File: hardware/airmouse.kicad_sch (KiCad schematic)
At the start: 25 parts, among them J1 USB_C_Receptacle_USB2.0_16P, J2 Conn_01x07_Pin, U1 XC6206PxxxMR, U2 MPU-9250, U3 STM32F103CBTx, Y1 8MHz

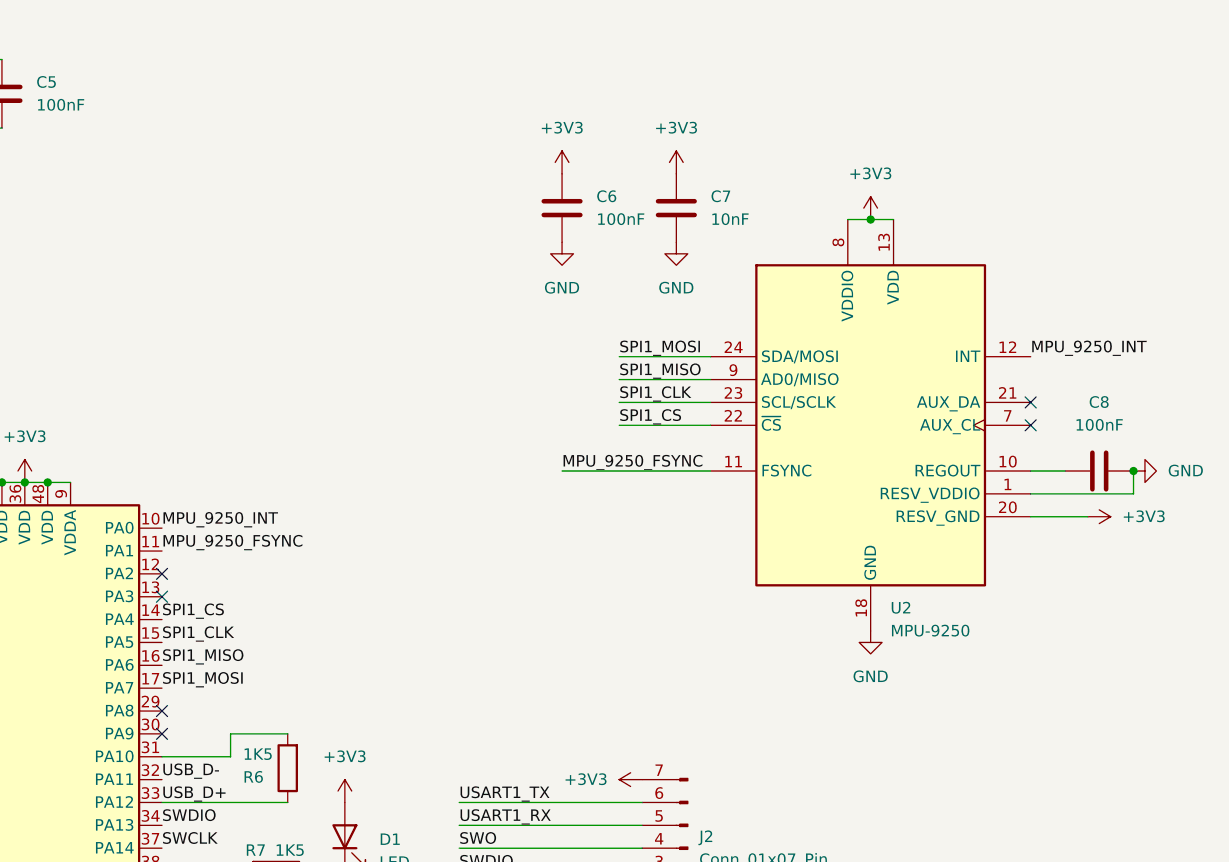
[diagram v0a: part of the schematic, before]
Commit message: 修改MPU-9250为ICM-20948
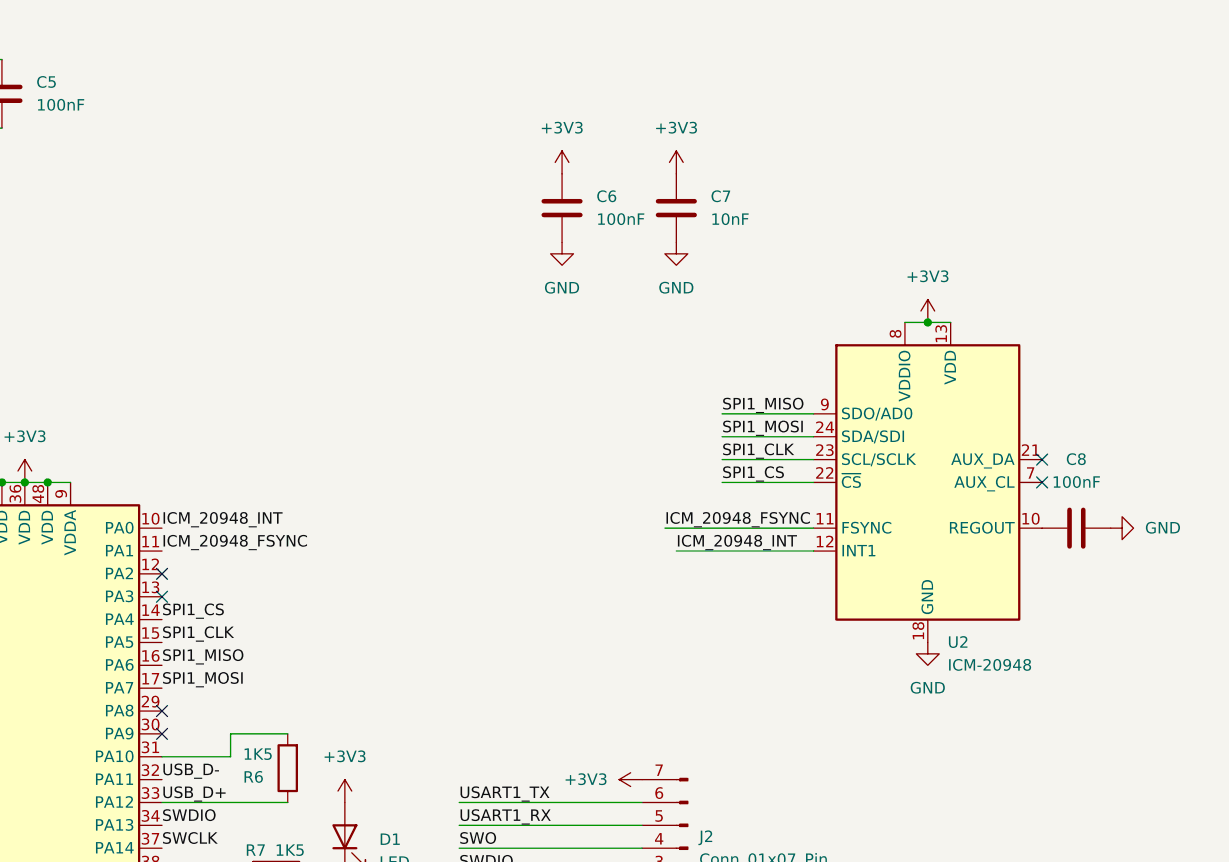
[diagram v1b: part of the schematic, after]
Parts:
- removed U2: MPU-9250, Sensor_Motion:InvenSense_QFN-24_3x3mm_P0.4mm, symbol Sensor_Motion:MPU-9250
- added U2: ICM-20948, Sensor_Motion:InvenSense_QFN-24_3x3mm_P0.4mm, symbol Sensor_Motion:ICM-20948
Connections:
- net +3V3: now also U2.13 (VDD), U2.8 (VDDIO)
- net GND: now also U2.18 (GND), U2.20 (GND)
- net SPI1_CLK: now also U2.23 (SCL/SCLK)
- net SPI1_CS: now also U2.22 (~{CS})
- net SPI1_MISO: now also U2.9 (SDO/AD0)
- net SPI1_MOSI: now also U2.24 (SDA/SDI)
- net at C8.1: now also U2.10 (REGOUT)
- net MPU_9250_FSYNC renamed ICM_20948_FSYNC
- net ICM_20948_FSYNC: now also U2.11 (FSYNC)
- net MPU_9250_INT renamed ICM_20948_INT
- net ICM_20948_INT: now also U2.12 (INT1)
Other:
- moved on the sheet: C8
